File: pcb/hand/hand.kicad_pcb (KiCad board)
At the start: 2 copper layers, 178.2 x 125.2 mm, 47 parts, among them J1 Conn_01x15, J2 Conn_01x15

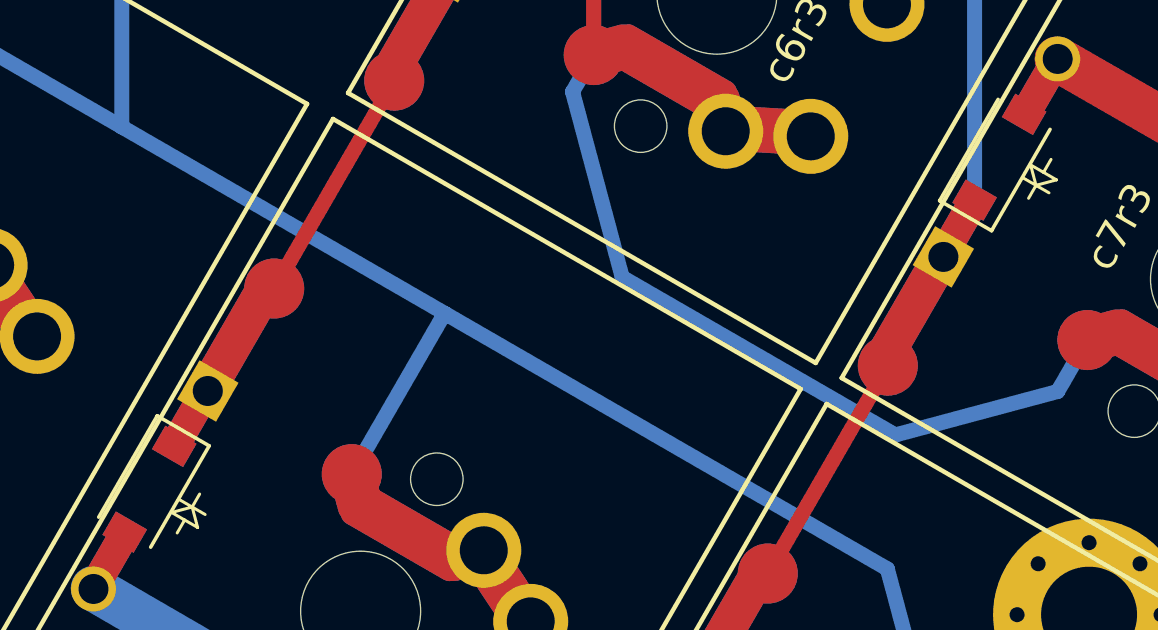
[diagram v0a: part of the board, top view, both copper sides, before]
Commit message: pcb/hand DRC connections
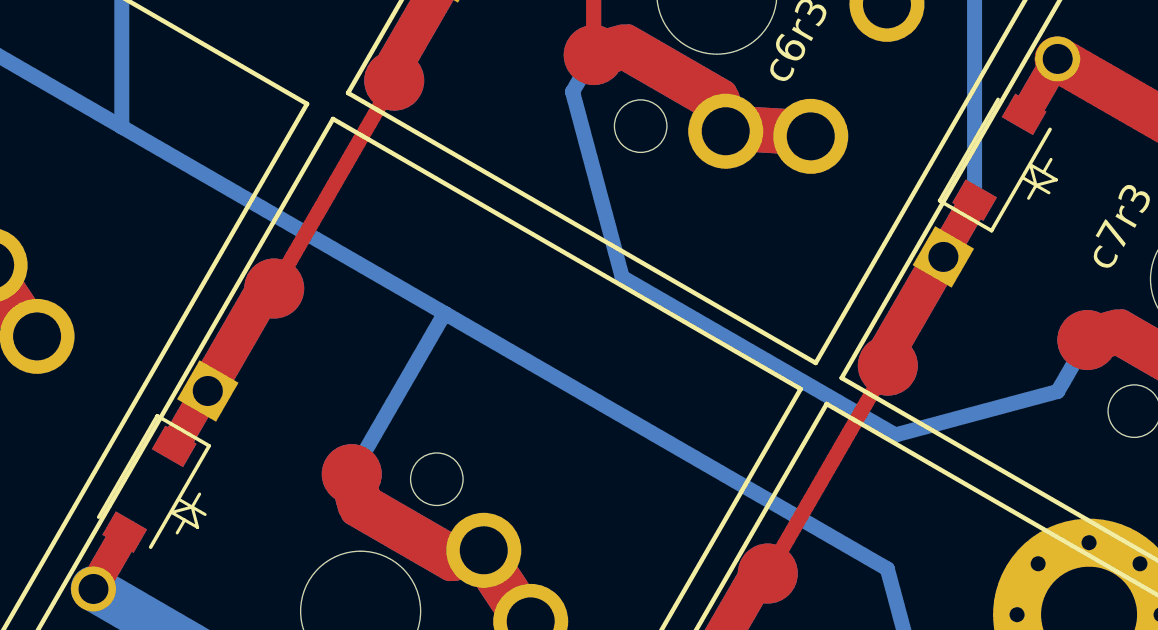
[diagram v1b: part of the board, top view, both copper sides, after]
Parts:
- 16mm (x2), 24mm, 6mm: footprint MountingHole:MountingHole_3.2mm_M3_Pad_Via -> hand:MountingHole_3.2mm_M3_Pad_Via
- J1, J2: footprint Connector_FFC-FPC:TE_1-84953-5_1x15-1MP_P1.0mm_Horizontal -> hand:TE_1-84953-5_1x15-1MP_P1.0mm_Horizontal
- LED1, LED2: footprint Diode_SMD:D_0603_1608Metric_Pad1.05x0.95mm_HandSolder -> hand:D_0603_1608Metric_Pad1.05x0.95mm_HandSolder
- R1, R2: footprint Resistor_SMD:R_0603_1608Metric_Pad0.98x0.95mm_HandSolder -> hand:R_0603_1608Metric_Pad0.98x0.95mm_HandSolder
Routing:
- net col7: track 73.9 -> 80.6 mm
- net col6: track 146.3 -> 152.3 mm

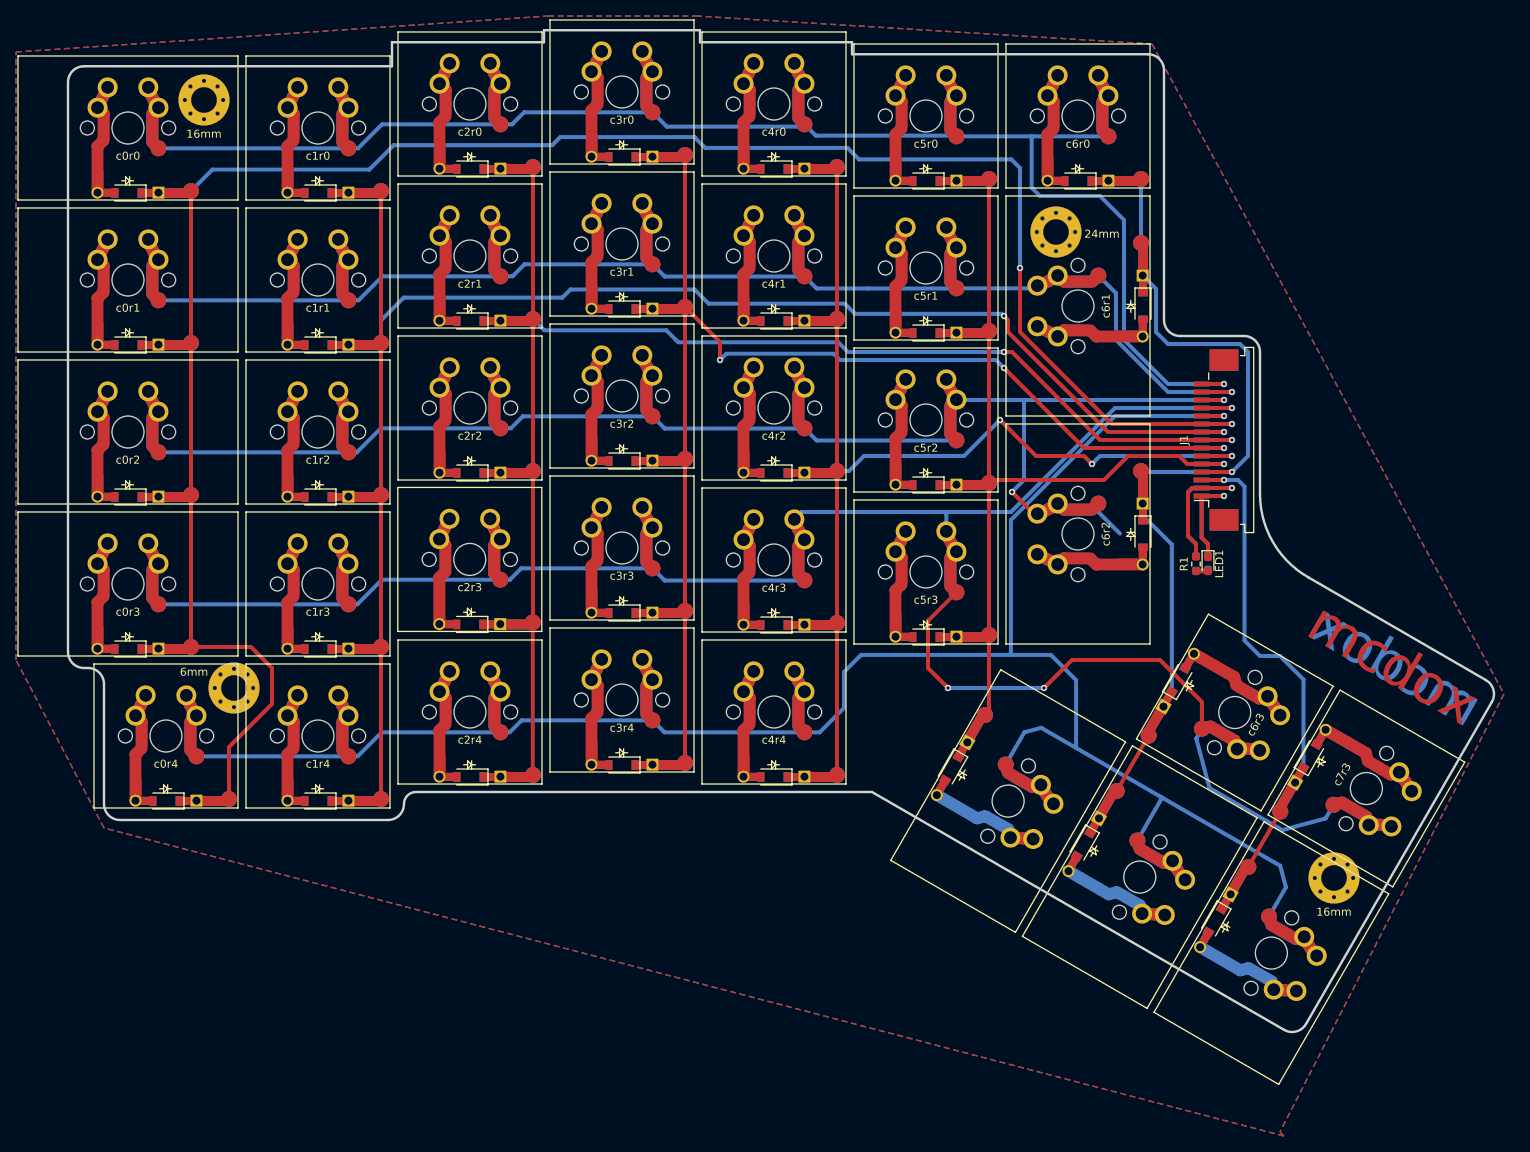
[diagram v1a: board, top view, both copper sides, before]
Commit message: pcb/hand Vanity features on one side only to save space.
Max dimensions 174x125.5mm
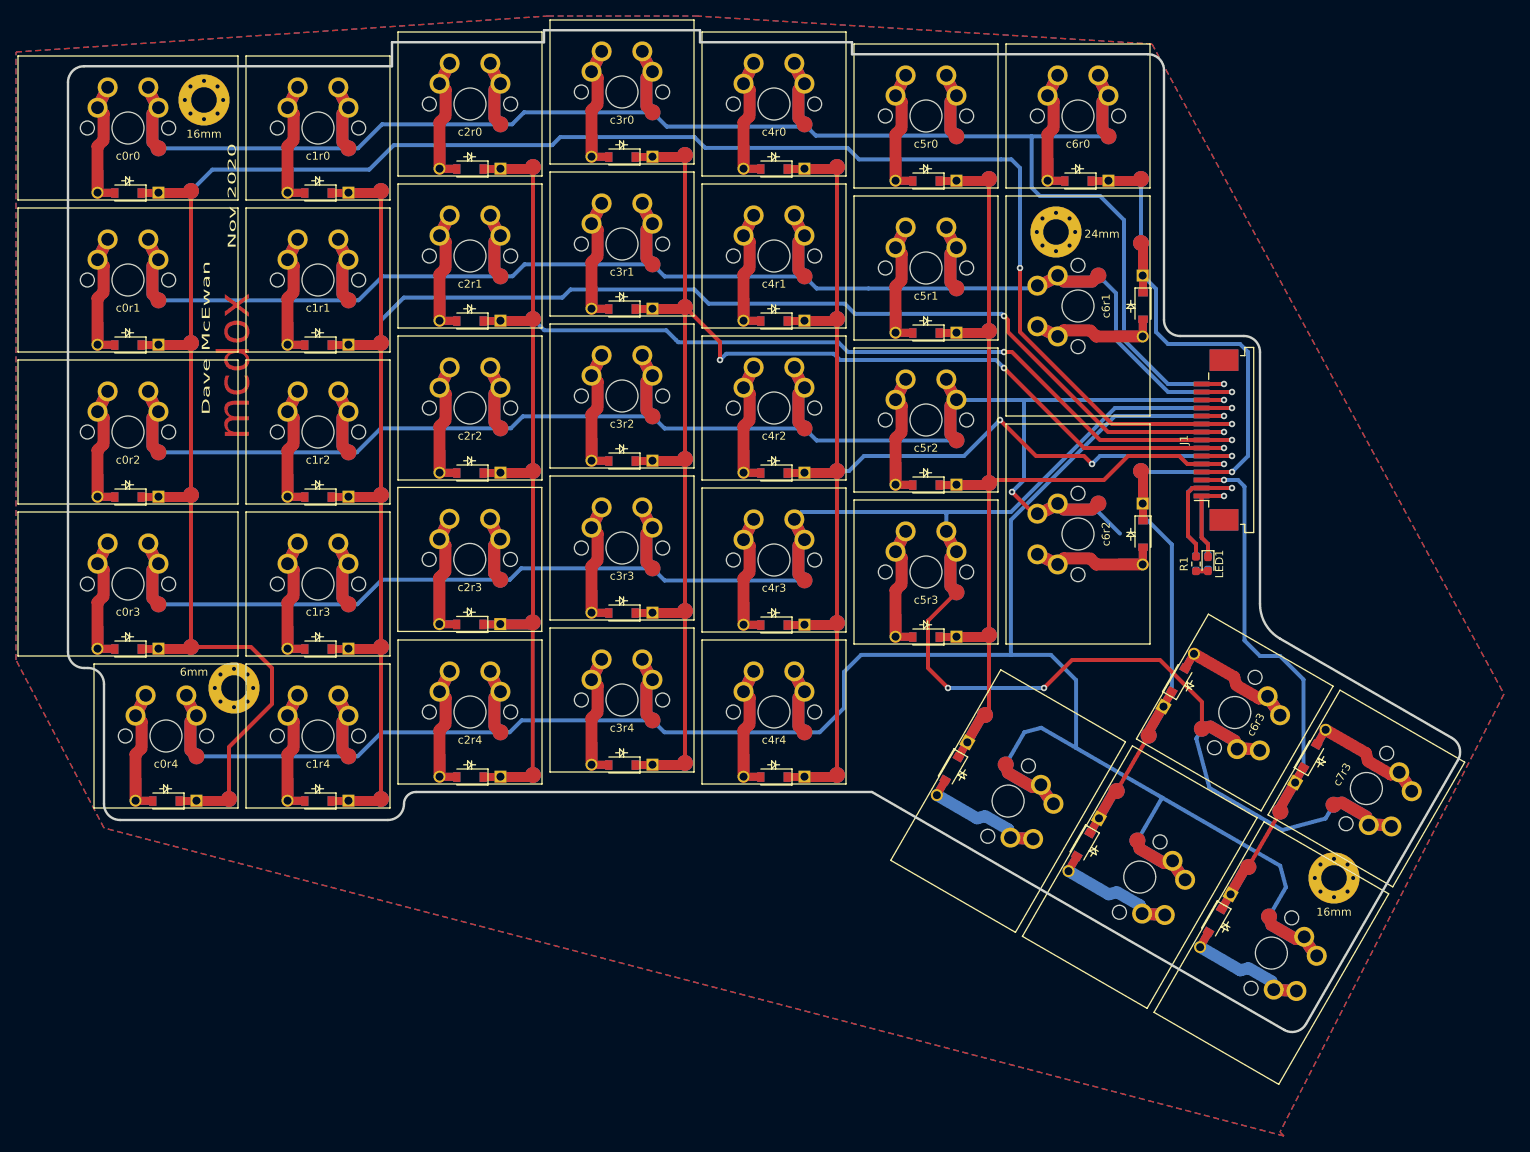
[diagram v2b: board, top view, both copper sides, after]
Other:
- board size 178.2 x 125.2 mm -> 174 x 125.2 mm
- board text added: "Dave McEwan"
- board text added: "Nov 2020"
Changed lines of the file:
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@@
   (general
     (thickness 1.6)
-    (drawings 37)
+    (drawings 38)
     (tracks 693)
     (zones 0)
@@
     (pad "" np_thru_hole circle (at 0 0) (size 4 4) (drill 4) (layers *.Cu *.Mask))
   )
+  (gr_text "Nov 2020" (at 57 47.5 90) (layer F.SilkS)
+    (effects (font (size 1 2) (thickness 0.15)))
+  )
+  (gr_text "Dave McEwan" (at 53.75 65.25 90) (layer F.SilkS)
+    (effects (font (size 1 2) (thickness 0.15)))
+  )
+  (gr_text mcdox (at 57.25 68.75 90) (layer F.Cu)
+    (effects (font (size 4 4) (thickness 0.3)))
+  )
   (gr_line (start 80 122) (end 137 122) (layer Edge.Cuts) (width 0.3))
-  (gr_arc (start 197.5 84.75) (end 185.5 84.75) (angle -60.2551187) (layer Edge.Cuts) (width 0.3))
+  (gr_arc (start 190.5 98.5) (end 185.5 98.5) (angle -60.30000583) (layer Edge.Cuts) (width 0.3))
   (gr_arc (start 80 123.5) (end 80 122) (angle -90) (layer Edge.Cuts) (width 0.3))
   (gr_arc (start 76.5 123.5) (end 76.5 125.5) (angle -90) (layer Edge.Cuts) (width 0.3))
   (gr_arc (start 189.51795 150) (end 188.51795 151.73205) (angle -90) (layer Edge.Cuts) (width 0.3))
-  (gr_arc (start 212.75 109.75) (end 214.48205 110.75) (angle -90) (layer Edge.Cuts) (width 0.3))
-  (gr_line (start 213.75 108.01795) (end 191.546333 95.168918) (layer Edge.Cuts) (width 0.3))
-  (gr_line (start 191.25 151) (end 214.48205 110.75) (layer Edge.Cuts) (width 0.3))
+  (gr_arc (start 208.5 117) (end 210.25 118) (angle -90) (layer Edge.Cuts) (width 0.3))
+  (gr_line (start 209.5 115.25) (end 188.022707 102.843158) (layer Edge.Cuts) (width 0.3))
+  (gr_line (start 191.25 151) (end 210.25 118) (layer Edge.Cuts) (width 0.3))
   (gr_line (start 137 122) (end 188.51795 151.73205) (layer Edge.Cuts) (width 0.3))
   (gr_line (start 133.5 90.5) (end 160 52) (layer Dwgs.User) (width 0.15))
   (gr_line (start 57 109) (end 90 60.75) (layer Dwgs.User) (width 0.15))
   (gr_line (start 53.5 35.5) (end 194.75 132.75) (layer Dwgs.User) (width 0.15))
-  (gr_text mcdox (at 202.562599 106.238221 -30) (layer B.Cu)
-    (effects (font (size 5 5) (thickness 0.3)) (justify mirror))
-  )
-  (gr_text mcdox (at 202.129587 105.988221 -30) (layer F.Cu)
-    (effects (font (size 5 5) (thickness 0.3)))
-  )
   (gr_arc (start 183.5 67) (end 185.5 67) (angle -90) (layer Edge.Cuts) (width 0.3))
   (gr_arc (start 175.5 63) (end 173.5 63) (angle -90) (layer Edge.Cuts) (width 0.3))
   (gr_arc (start 171.5 31.778) (end 173.5 31.778) (angle -90) (layer Edge.Cuts) (width 0.3))
   (gr_line (start 38.5 106.5) (end 39 106.5) (layer Edge.Cuts) (width 0.3))
-  (gr_line (start 185.5 67) (end 185.5 84.75) (layer Edge.Cuts) (width 0.3))
+  (gr_line (start 185.5 67) (end 185.5 98.5) (layer Edge.Cuts) (width 0.3))
   (gr_line (start 175.5 65) (end 183.5 65) (layer Edge.Cuts) (width 0.3))
   (gr_line (start 173.5 31.778) (end 173.5 63) (layer Edge.Cuts) (width 0.3))
@@
   (segment (start 178.925 94.325) (end 179 94.25) (width 0.5) (layer B.Cu) (net 17))
   (segment (start 177.5 94.325) (end 178.925 94.325) (width 0.5) (layer B.Cu) (net 17))
-  (zone (net 0) (net_name "") (layers F&B.Cu) (hatch edge 0.508)
-    (connect_pads (clearance 0.508))
-    (min_thickness 0.254)
-    (keepout (tracks allowed) (vias allowed) (copperpour not_allowed))
-    (fill (arc_segments 32) (thermal_gap 0.508) (thermal_bridge_width 0.508))
-    (polygon
-      (pts
-        (xy 211.454904 114.836297) (xy 190.237282 102.586297) (xy 193.487282 96.957132) (xy 214.704903 109.207132)
-      )
-    )
-  )
   (zone (net 0) (net_name "") (layer F.Cu) (hatch edge 0.508)
     (connect_pads (clearance 1))
@@
       )
     )
+  )
+  (zone (net 0) (net_name "") (layer F.Cu) (hatch edge 0.508)
+    (connect_pads (clearance 1))
+    (min_thickness 0.254)
+    (keepout (tracks allowed) (vias allowed) (copperpour not_allowed))
+    (fill (arc_segments 32) (thermal_gap 0.508) (thermal_bridge_width 0.508))
+    (polygon
+      (pts
+        (xy 60 78.5) (xy 54.5 78.5) (xy 54.5 58.5) (xy 60 58.5)
+      )
+    )

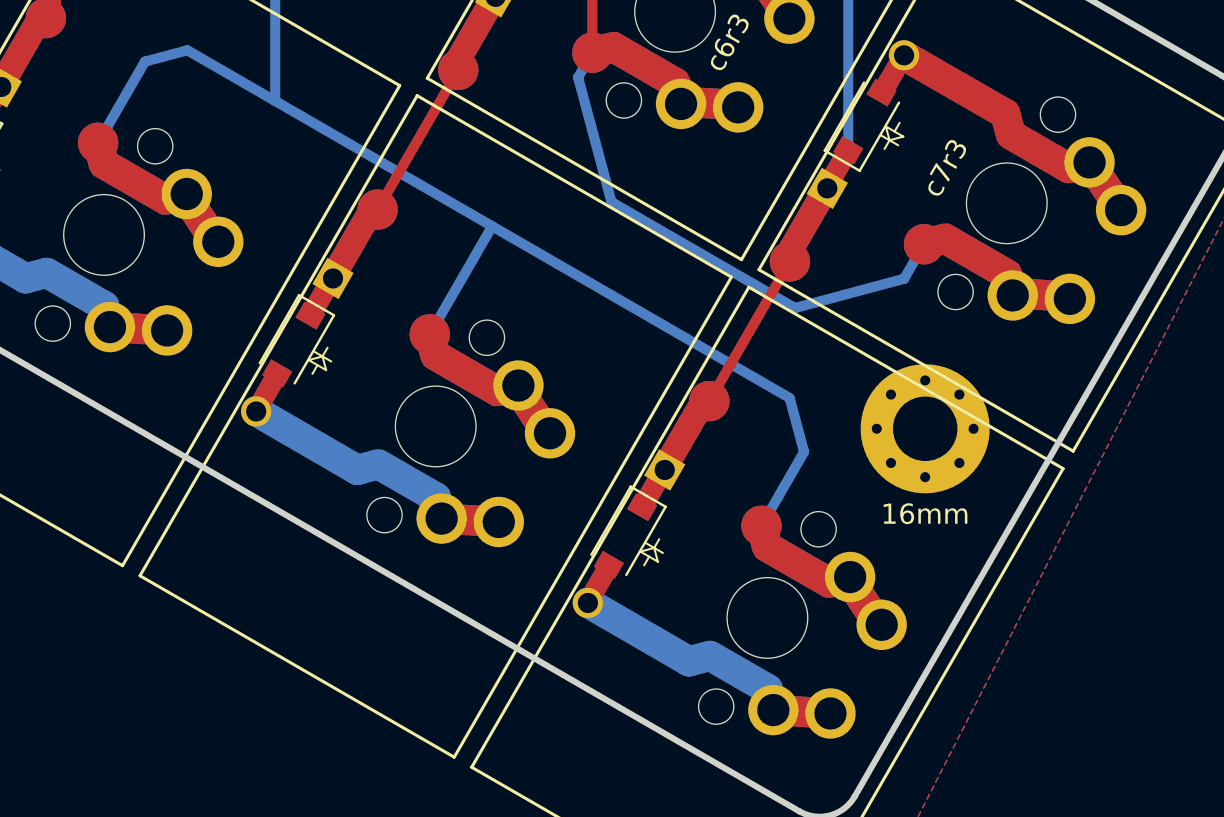
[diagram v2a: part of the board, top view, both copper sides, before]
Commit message: pcb/hand Label c*r* on both sides
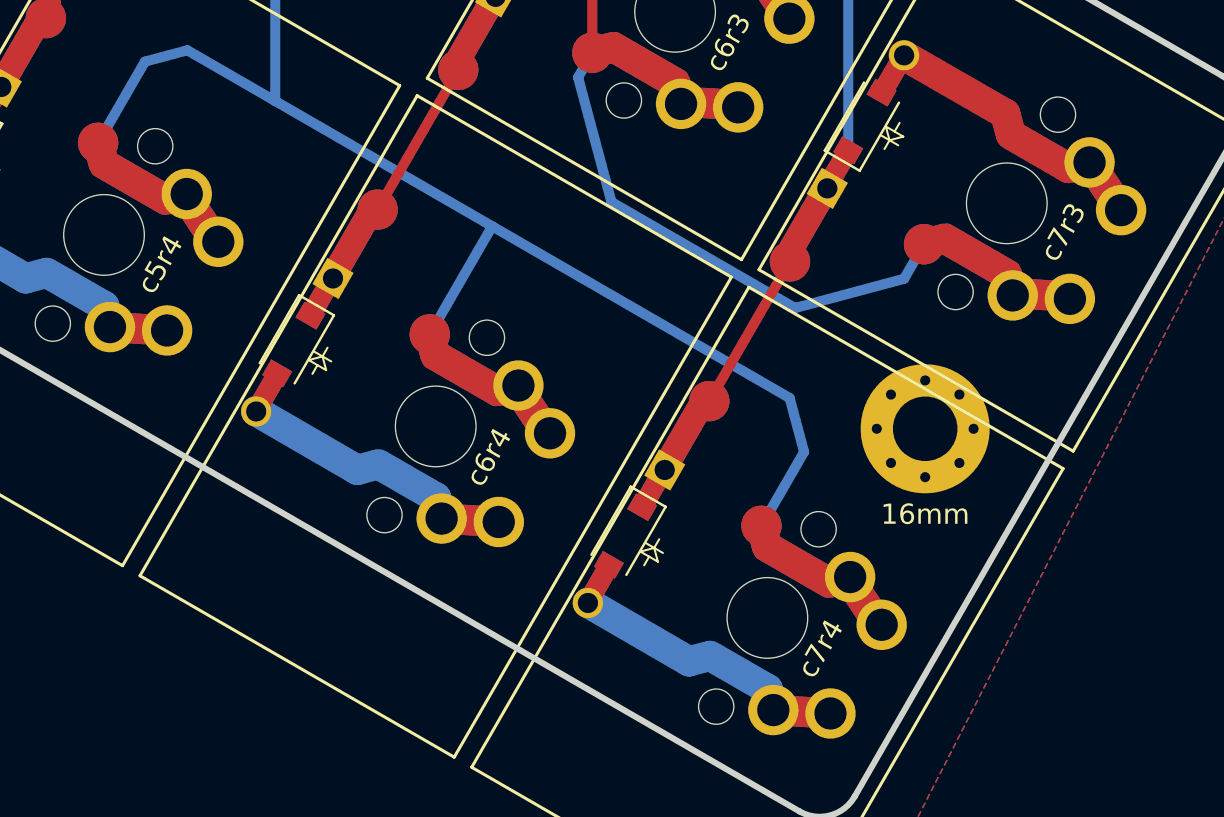
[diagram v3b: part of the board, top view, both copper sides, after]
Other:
- board text added: "c0r5"
- board text added: "c0r6"
- board text added: "c0r7"
- board text added: "c0r8"
- board text added: "c0r9"
- board text added: "c1r5"
- board text added: "c1r6"
- board text added: "c1r7"
- board text added: "c1r8"
- board text added: "c1r9"
- board text added: "c2r5"
- board text added: "c2r6"
- board text added: "c2r7"
- board text added: "c2r8"
- board text added: "c2r9"
- board text added: "c3r5"
- board text added: "c3r6"
- board text added: "c3r7"
- board text added: "c3r8"
- board text added: "c3r9"
- board text added: "c4r5"
- board text added: "c4r6"
- board text added: "c4r7"
- board text added: "c4r8"
- board text added: "c4r9"
- board text added: "c5r5"
- board text added: "c5r6"
- board text added: "c5r7"
- board text added: "c5r8"
- board text added: "c5r9"
- board text added: "c6r5"
- board text added: "c6r6"
- board text added: "c6r7"
- board text added: "c6r8"
- board text added: "c6r9"
- board text added: "c7r5"
- board text added: "c7r6"
